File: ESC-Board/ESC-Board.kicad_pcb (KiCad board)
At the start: 2 copper layers, 162 x 68 mm, 27 parts, among them J1 Molex, J2 Molex, J3 XT_60, U1 ACS780xLRTR-100U, U10 TMP235A2DBZT, U2 ACS780xLRTR-100U, U3 ACS780xLRTR-100U, U4 ACS780xLRTR-100U, U5 ESC:Blue_ESC, U6 ESC:Blue_ESC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

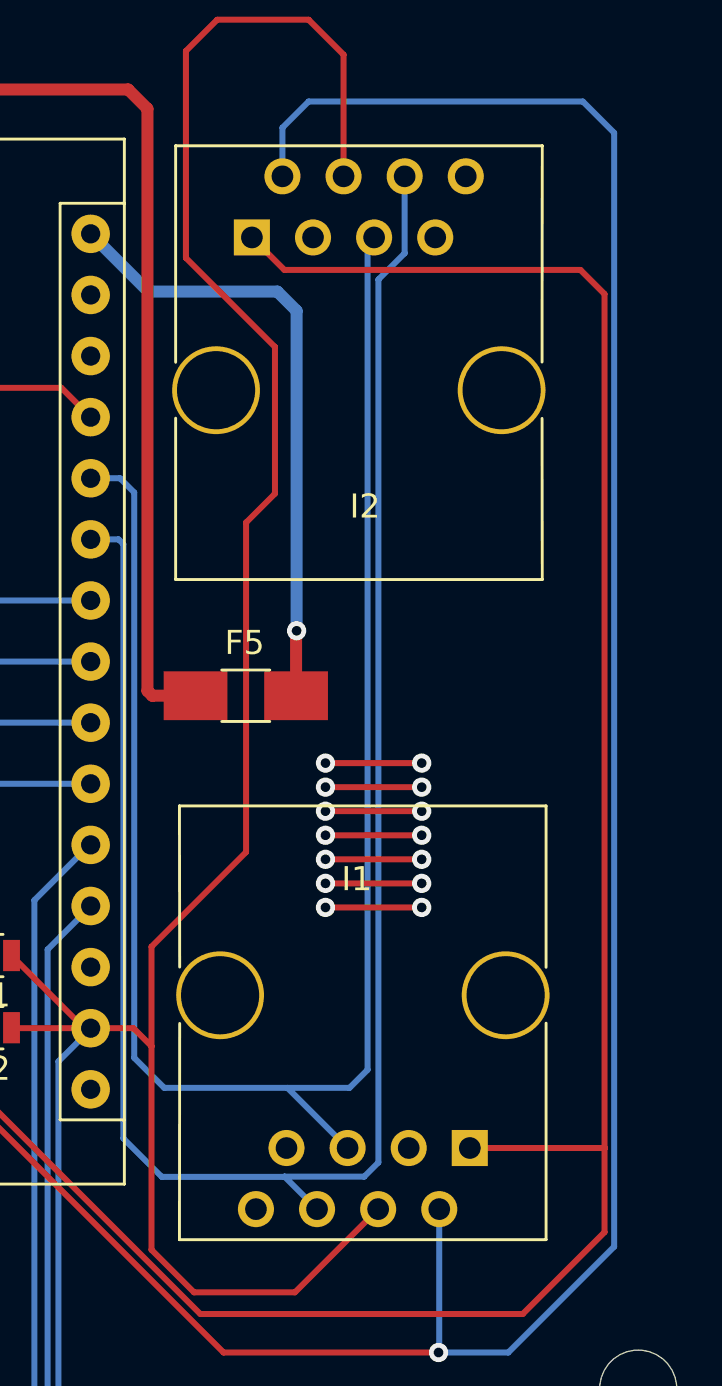
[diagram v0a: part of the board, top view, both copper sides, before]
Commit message: Fixed RJ 45 connector
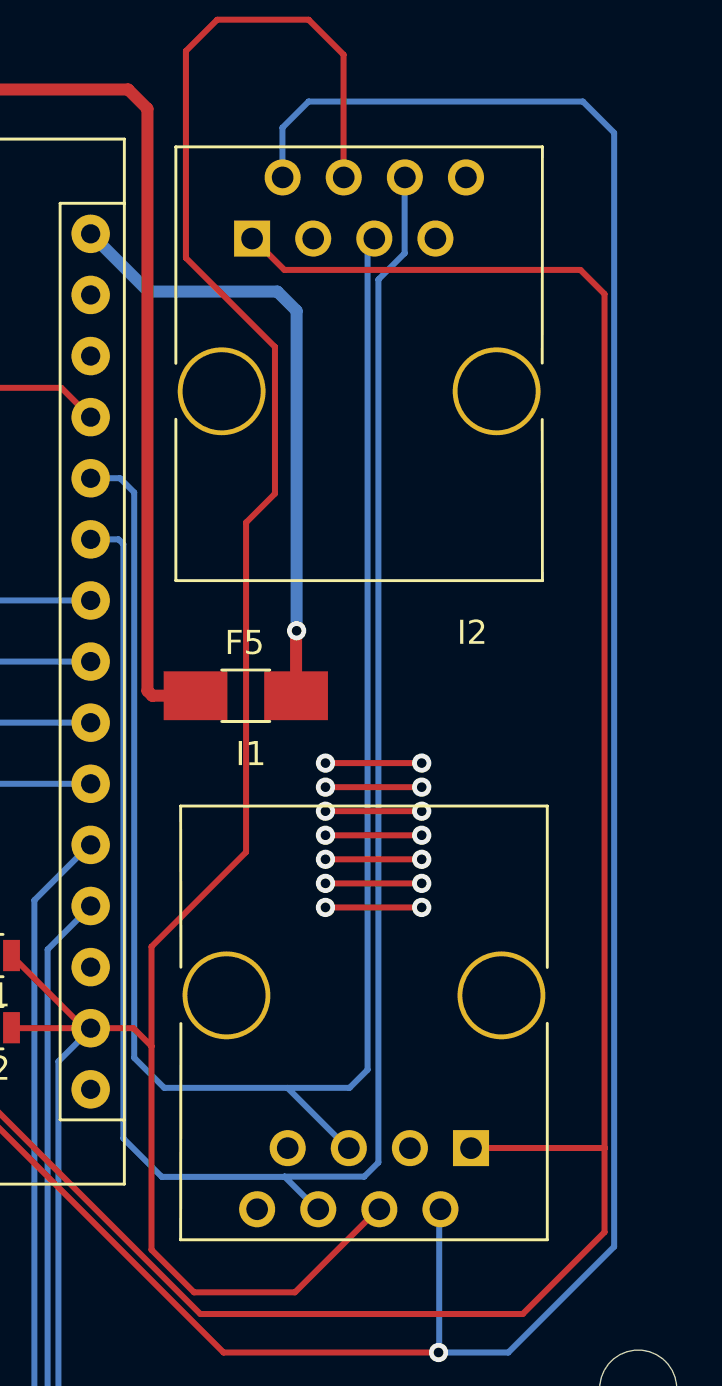
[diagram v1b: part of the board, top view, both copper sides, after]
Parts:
- I1, I2: footprint Connectors:RJ45_8 -> Blue_ESC:RJ45_8
- moved I2 6.89 mm to (175.4, 62.4)
- moved I1 6.81 mm to (175.6, 89.8)

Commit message: Fixed PDU footprint isuess
vicor foot print fixed
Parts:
-  MH3: renamed from MH3
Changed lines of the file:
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@@
     (tags "mounting hole 3.2mm no annular m3")
     (attr virtual)
-    (fp_text reference MH3 (at 0 -4.2) (layer F.SilkS) hide
+    (fp_text reference " MH3" (at 0 -4.2) (layer F.SilkS) hide
       (effects (font (size 1 1) (thickness 0.15)))
     )

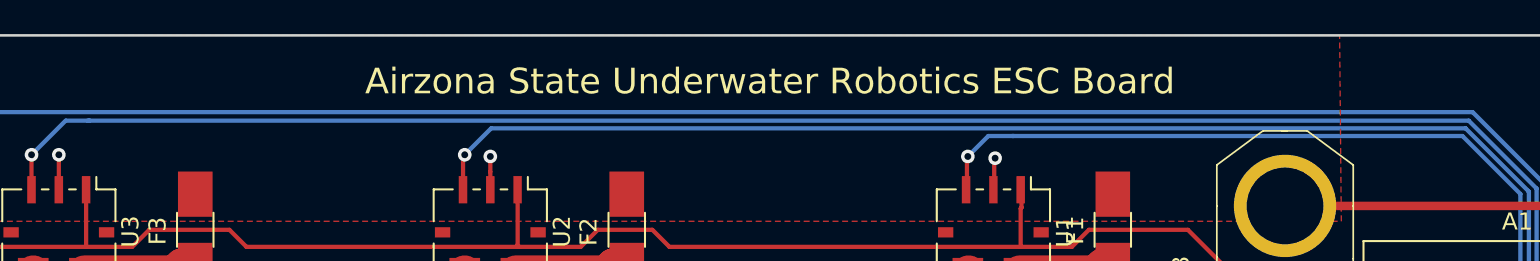
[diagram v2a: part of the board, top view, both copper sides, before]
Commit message: Added Drill files and fixed holes
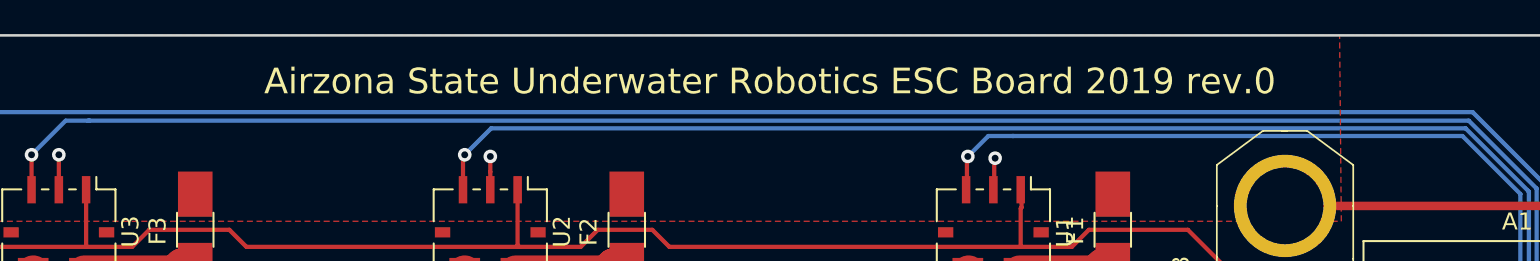
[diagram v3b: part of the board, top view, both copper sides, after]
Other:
- board text added: "Airzona State Underwater Robotics ESC Board 2019 rev.0"
- board text removed: "Airzona State Underwater Robotics ESC Board"
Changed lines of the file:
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@@
       (net 3 GND))
   )
-  (gr_text "Airzona State Underwater Robotics ESC Board\n" (at 112.8 43.7) (layer F.SilkS)
+  (gr_text "Airzona State Underwater Robotics ESC Board 2019 rev.0\n" (at 112.8 43.7) (layer F.SilkS)
     (effects (font (size 1.5 1.5) (thickness 0.3)))
   )

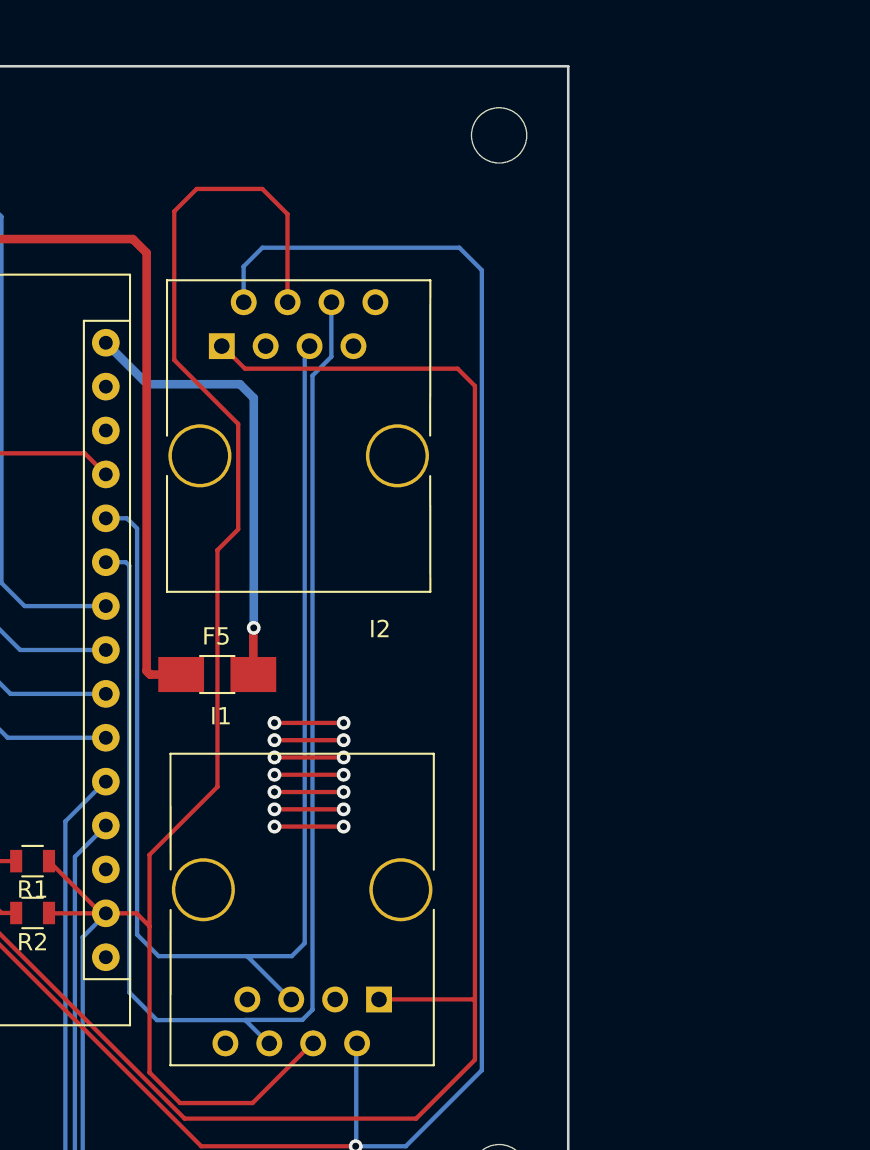
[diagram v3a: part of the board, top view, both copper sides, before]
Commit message: Updated PDU and ESC for leak sensor
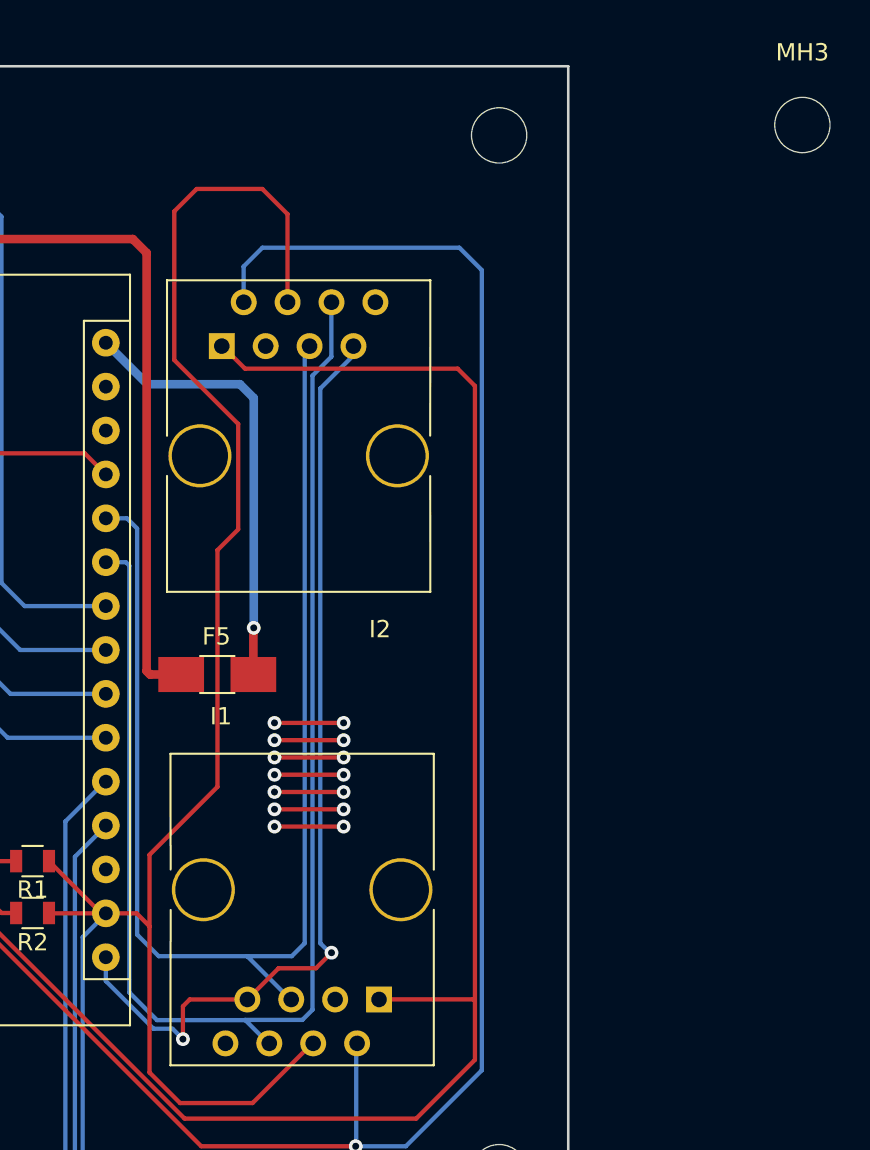
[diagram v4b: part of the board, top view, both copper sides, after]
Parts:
- added MH3: MountingHole, Mounting_Holes:MountingHole_3.2mm_M3, F.Cu at (204.6, 44.4)
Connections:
- A1 pad 16: Net-(A1-Pad16) -> EXT_Water_Sensor
- I1 pad 7: Net-(I1-Pad7) -> EXT_Water_Sensor
- I2 pad 7: Net-(I2-Pad7) -> EXT_Water_Sensor
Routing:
- net EXT_Water_Sensor: track 0.00 -> 55.2 mm, vias 0 -> 2

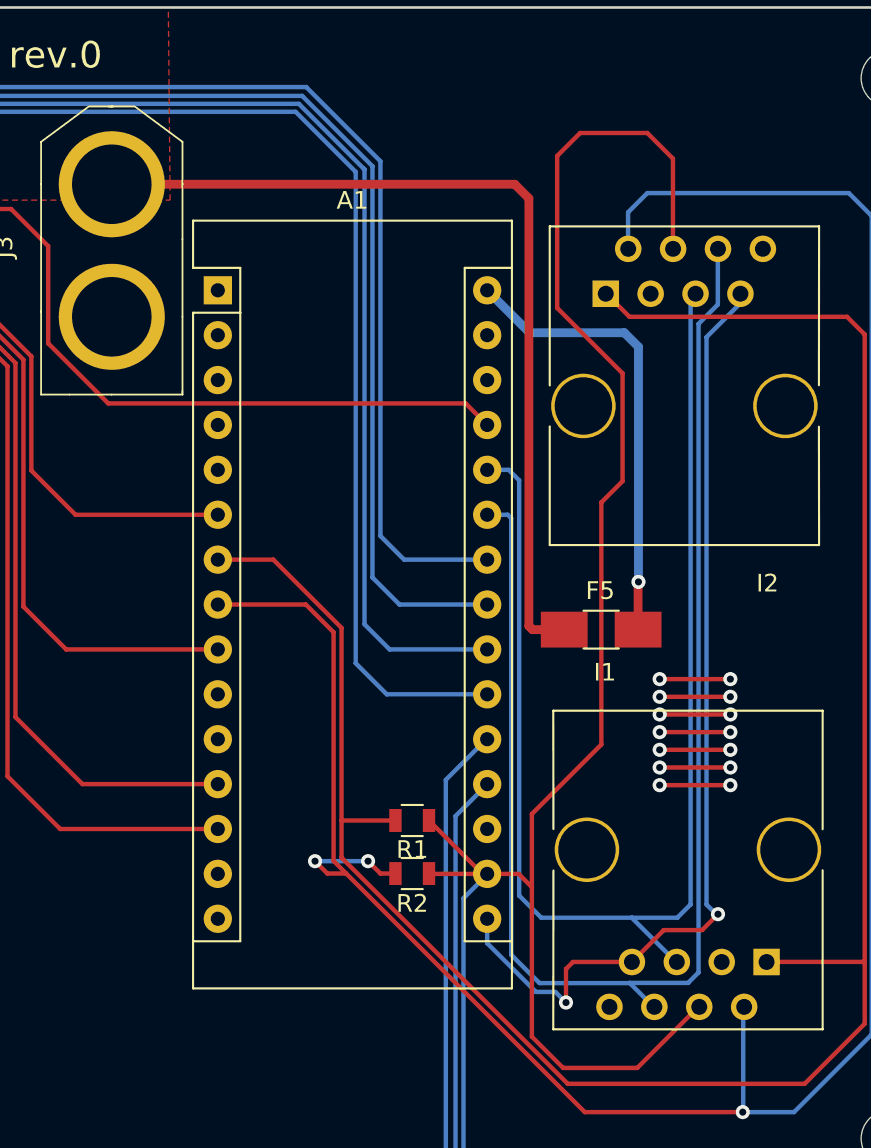
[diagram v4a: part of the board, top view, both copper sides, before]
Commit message: Added 5v
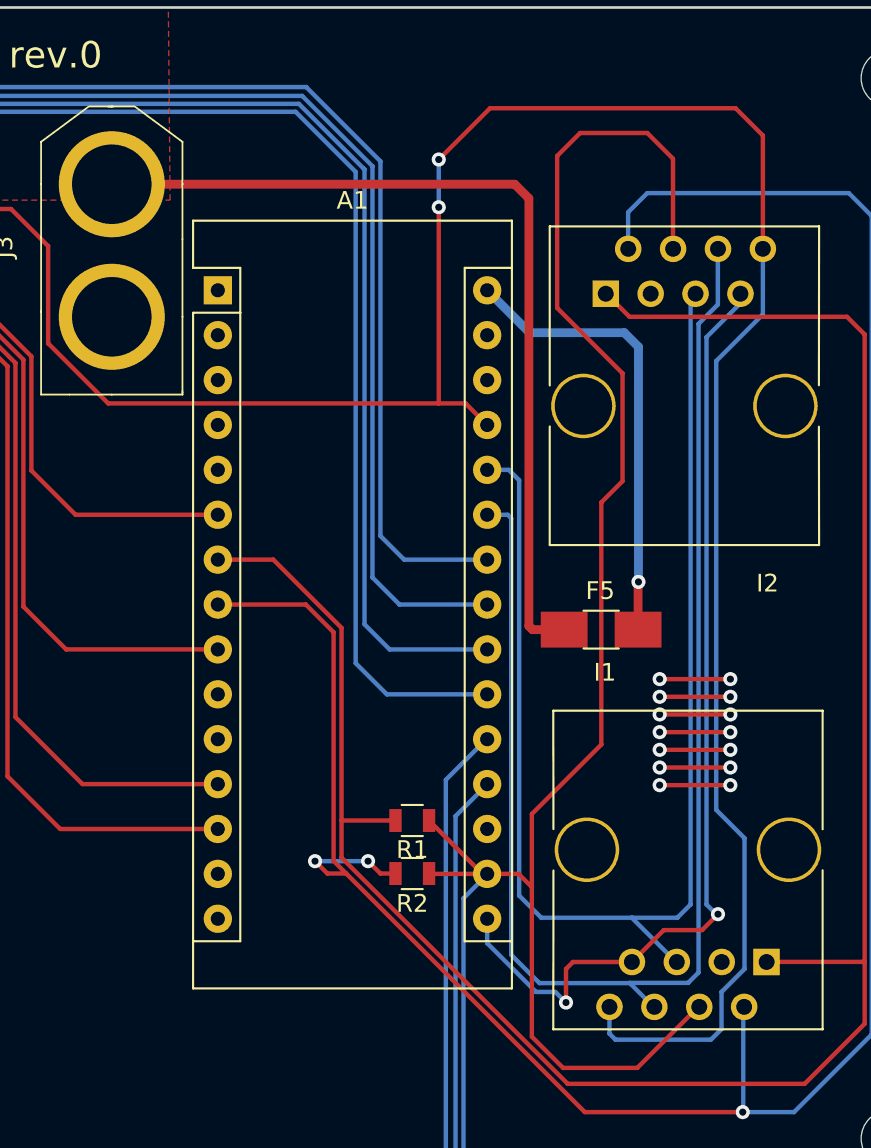
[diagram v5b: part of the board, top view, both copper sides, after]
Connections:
- I1 pad 8: Net-(I1-Pad8) -> +5V
- I2 pad 8: Net-(I2-Pad8) -> +5V
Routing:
- net +5V: track 143.6 -> 238.7 mm, vias 0 -> 2

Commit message: Finalized
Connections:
- A1 pad 14: Net-(A1-Pad14) -> EXT_PWM_LED
- A1 pad 16: EXT_Water_Sensor -> Net-(A1-Pad16)
- I1 pad 7: EXT_Water_Sensor -> EXT_PWM_LED
- I2 pad 7: EXT_Water_Sensor -> EXT_PWM_LED
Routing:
- net EXT_PWM_LED: track 0.00 -> 69.6 mm, vias 0 -> 4
- net EXT_Water_Sensor: track 55.2 -> 0.00 mm, vias 2 -> 0
- net GND: track 43.0 -> 47.9 mm, vias 22 -> 23
